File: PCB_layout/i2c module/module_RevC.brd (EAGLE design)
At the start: 33.3 x 50.2 mm, 86 parts, among them IC1 ATTINY85-20SU, J1 M20-9980346

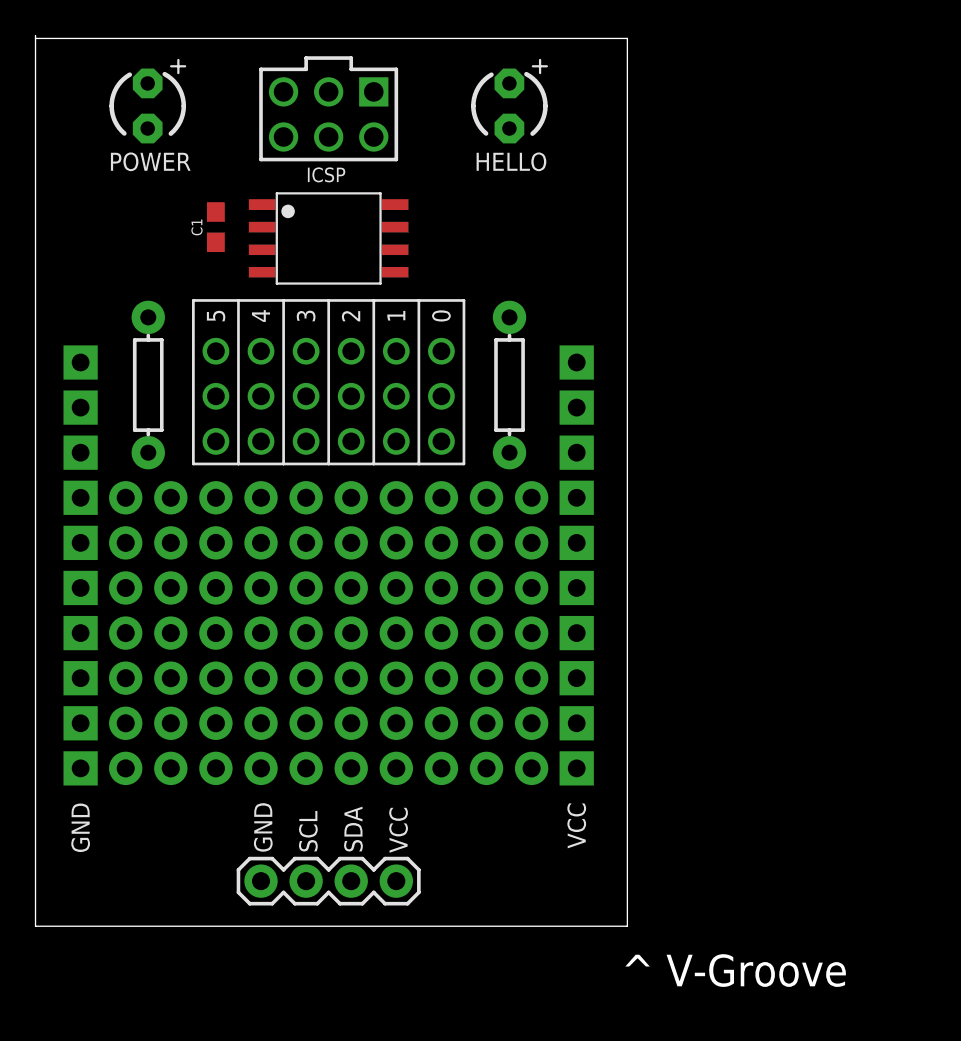
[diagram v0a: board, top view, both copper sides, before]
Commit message: added i2c rev C
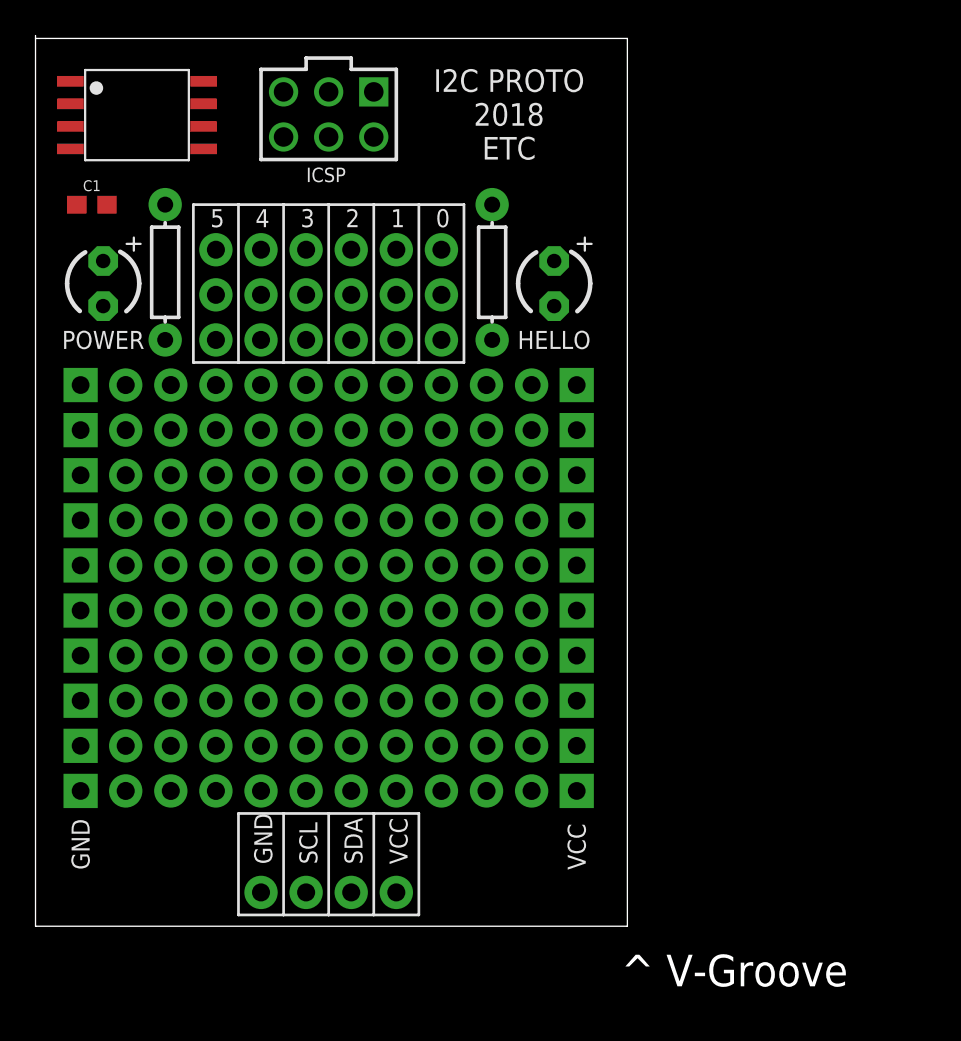
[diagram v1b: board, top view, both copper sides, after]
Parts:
- removed 0, 1, 2, 3, 4, 5: 3X-PADS-CONNECTED, BadgeParts:3X-PADS
- removed J2: (no value), SparkFun-Connectors:1X04
- added U$100, U$101, U$102, U$103, U$104, U$105, U$106, U$107, U$108, U$109, U$110, U$111, U$112, U$113, U$114, U$115, U$116, U$117, U$118, U$119, U$120, U$121, U$122, U$75, U$76, U$77, U$78, U$79, U$80, U$81, U$82, U$83, U$84, U$85, U$86, U$87, U$88, U$89, U$90, U$91, U$92, U$93, U$94, U$95, U$96, U$97, U$98, U$99: ONE_PAD, BadgeParts:1X01
- added U$71: GND, BadgeParts:1X01
- added U$72: SDA, BadgeParts:1X01
- added U$73: SCL, BadgeParts:1X01
- added U$74: VCC, BadgeParts:1X01
- moved IC1 12.8 mm to (5.71, 45.7)
- moved HELLO 10.3 mm to (29.2, 36.2)
- moved POWER 10.3 mm to (3.81, 36.2)
- moved C1 7.10 mm to (3.17, 40.6), turned to 0 degrees
- moved R2 6.42 mm to (25.7, 36.8), turned to 270 degrees
- moved R1 6.42 mm to (7.30, 36.8), turned to 270 degrees
- moved U$1 1.27 mm to (7.62, 15.2)
- moved U$10 1.27 mm to (7.62, 12.7)
- moved U$24 1.27 mm to (10.2, 15.2)
- moved U$25 1.27 mm to (12.7, 15.2)
- moved U$27 1.27 mm to (10.2, 12.7)
- moved U$28 1.27 mm to (12.7, 12.7)
- moved U$41 1.27 mm to (15.2, 15.2)
- moved U$42 1.27 mm to (17.8, 15.2)
- moved U$43 1.27 mm to (20.3, 15.2)
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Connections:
- net GND: now also U$71.1; no longer J2.1
- net PB0: now also U$72.1, U$75.1, U$76.1, U$77.1; no longer 0.P$1, 0.P$2, 0.P$3, J2.3
- net PB1: now also U$78.1, U$79.1, U$80.1; no longer 1.P$1, 1.P$2, 1.P$3
- net PB2: now also U$73.1, U$81.1, U$82.1, U$83.1; no longer 2.P$1, 2.P$2, 2.P$3, J2.2
- net PB3: now also U$84.1, U$85.1, U$86.1; no longer 3.P$1, 3.P$2, 3.P$3
- net PB4: now also U$87.1, U$88.1, U$89.1; no longer 4.P$1, 4.P$2, 4.P$3
- net PB5: now also U$90.1, U$91.1, U$92.1; no longer 5.P$1, 5.P$2, 5.P$3
- net VCC: now also U$74.1; no longer J2.4
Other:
- board text added: "0"
- board text added: "1"
- board text added: "2"
- board text added: "3"
- board text added: "4"
- board text added: "5"
- board text added: "I2C PROTO 2018 ETC"

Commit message: updated brd tsilk and added bitly link on bsilk, routed for SEEED
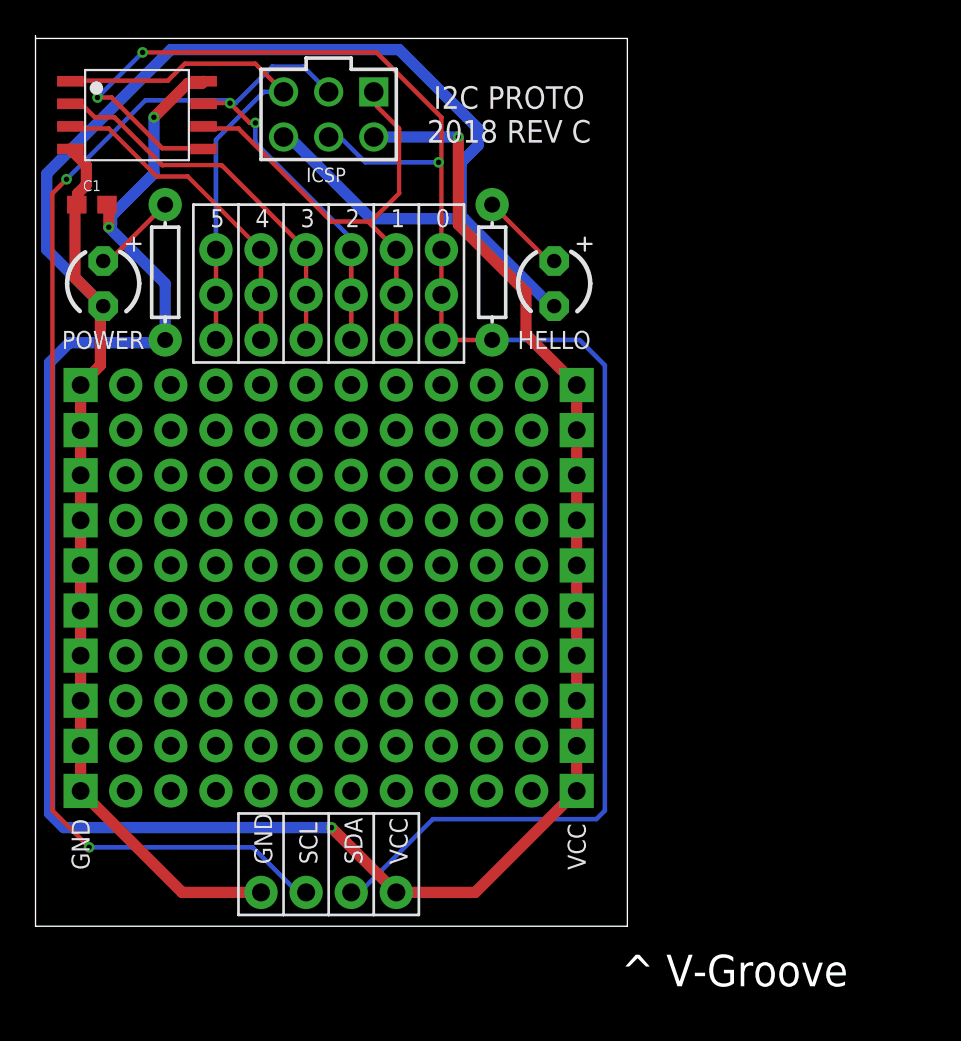
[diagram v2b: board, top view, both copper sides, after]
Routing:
- net VCC: track 0.00 -> 130.6 mm, vias 0 -> 4
- net GND: track 0.00 -> 113.0 mm
- net PB0: track 0.00 -> 99.7 mm, vias 0 -> 3
- net PB2: track 0.00 -> 88.0 mm, vias 0 -> 4
- net PB5: track 0.00 -> 29.3 mm
- net PB1: track 0.00 -> 27.5 mm
- net PB3: track 0.00 -> 21.8 mm
- net PB4: track 0.00 -> 18.7 mm
- net N$3: track 0.00 -> 4.81 mm
- net N$1: track 0.00 -> 4.81 mm
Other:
- board text added: "HOKANSON/BONTRAGER BIT.LY/BADGECULTURE"
- board text added: "I2C PROTO 2018 REV C"
- board text removed: "I2C PROTO 2018 ETC"

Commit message: compulsive text alignment
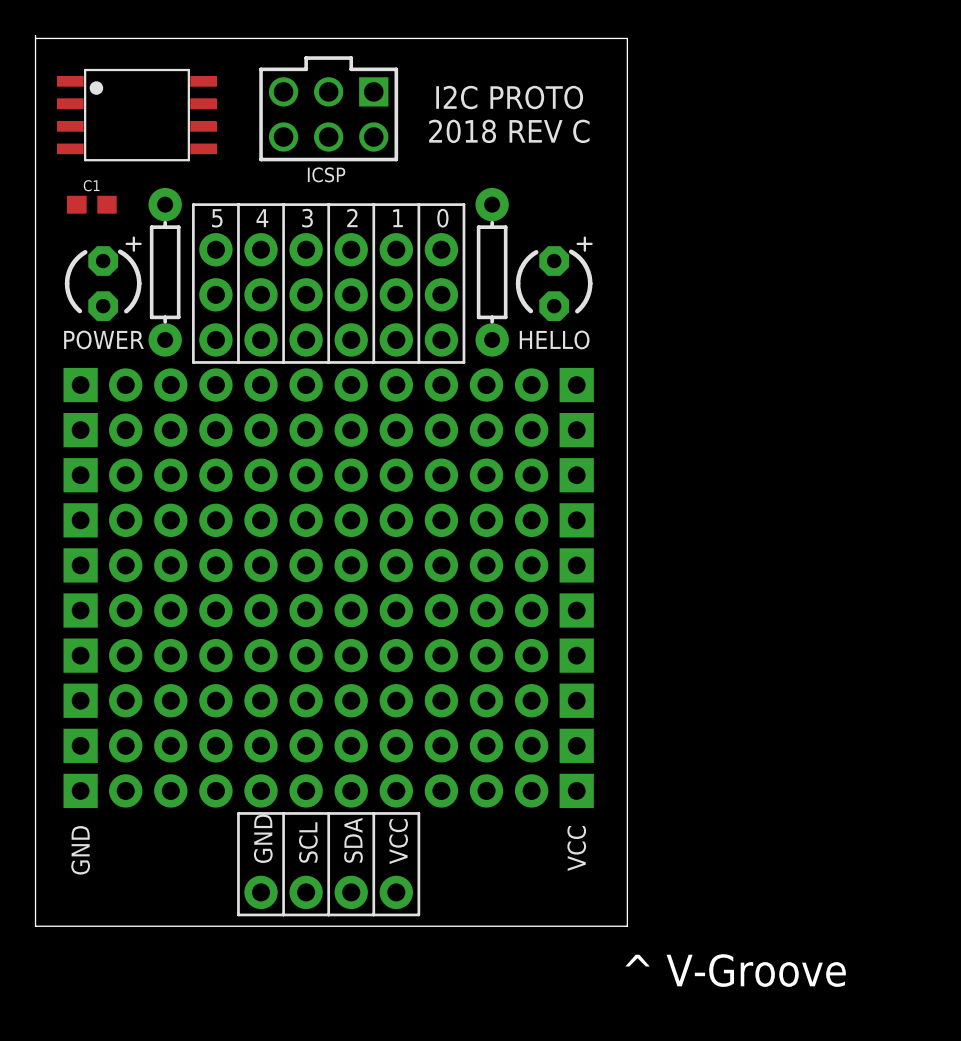
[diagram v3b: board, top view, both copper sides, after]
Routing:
- net VCC: track 130.6 -> 0.00 mm, vias 4 -> 0
- net GND: track 113.0 -> 0.00 mm
- net PB0: track 99.7 -> 0.00 mm, vias 3 -> 0
- net PB2: track 88.0 -> 0.00 mm, vias 4 -> 0
- net PB5: track 29.3 -> 0.00 mm
- net PB1: track 27.5 -> 0.00 mm
- net PB3: track 21.8 -> 0.00 mm
- net PB4: track 18.7 -> 0.00 mm
- net N$3: track 4.81 -> 0.00 mm
- net N$1: track 4.81 -> 0.00 mm

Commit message: fixed duplicate RST reference in ICSP definition
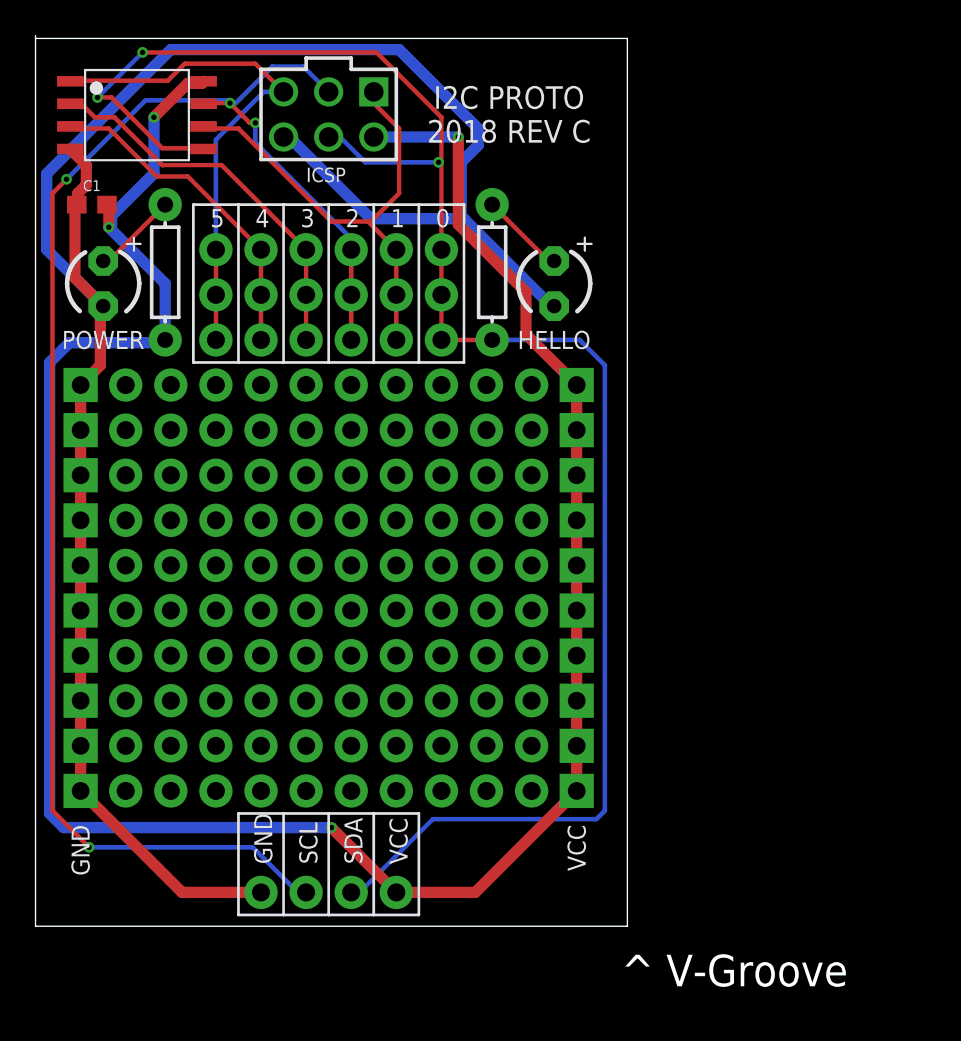
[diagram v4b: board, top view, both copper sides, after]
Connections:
- net PB1: now also J1.1/MISO; no longer J1.1/RST
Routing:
- net VCC: track 0.00 -> 130.6 mm, vias 0 -> 4
- net GND: track 0.00 -> 113.0 mm
- net PB0: track 0.00 -> 99.7 mm, vias 0 -> 3
- net PB2: track 0.00 -> 88.0 mm, vias 0 -> 4
- net PB5: track 0.00 -> 29.3 mm
- net PB1: track 0.00 -> 27.5 mm
- net PB3: track 0.00 -> 21.8 mm
- net PB4: track 0.00 -> 18.7 mm
- net N$3: track 0.00 -> 4.81 mm
- net N$1: track 0.00 -> 4.81 mm
